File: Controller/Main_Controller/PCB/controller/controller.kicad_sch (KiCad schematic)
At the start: 253 parts, among them J1 Conn_01x10, M1 Motor_DC, Q1 S9013, Q10 S9013, Q11 S9013, Q12 S9013, Q13 S9013, Q14 S9013, Q15 S9013, Q16 S9013, Q17 S9013, Q18 S9013, Q19 S9013, Q2 S9013, Q20 S9013, Q21 S9013, Q22 S9013, Q23 S9013, Q24 S9013, Q25 Q_PMOS_DGS, Q26 Q_NMOS_DGS, Q27 S9013, Q3 S9013, Q4 S9013, Q5 S9013, Q6 S9013, Q7 S9013, Q8 S9013, Q9 S9013, SW1 SW_SPDT, SW2 SW_SPDT, U1 NUCLEO-L432KC, U10 ZLDO1117G50TA, U2 NUCLEO144-F429ZI, U3 74HC14, U4 74HC14, U5 74HC14, U6 Joystick, U7 Joystick, U8 HY1602E, U9 ZSR330GTA

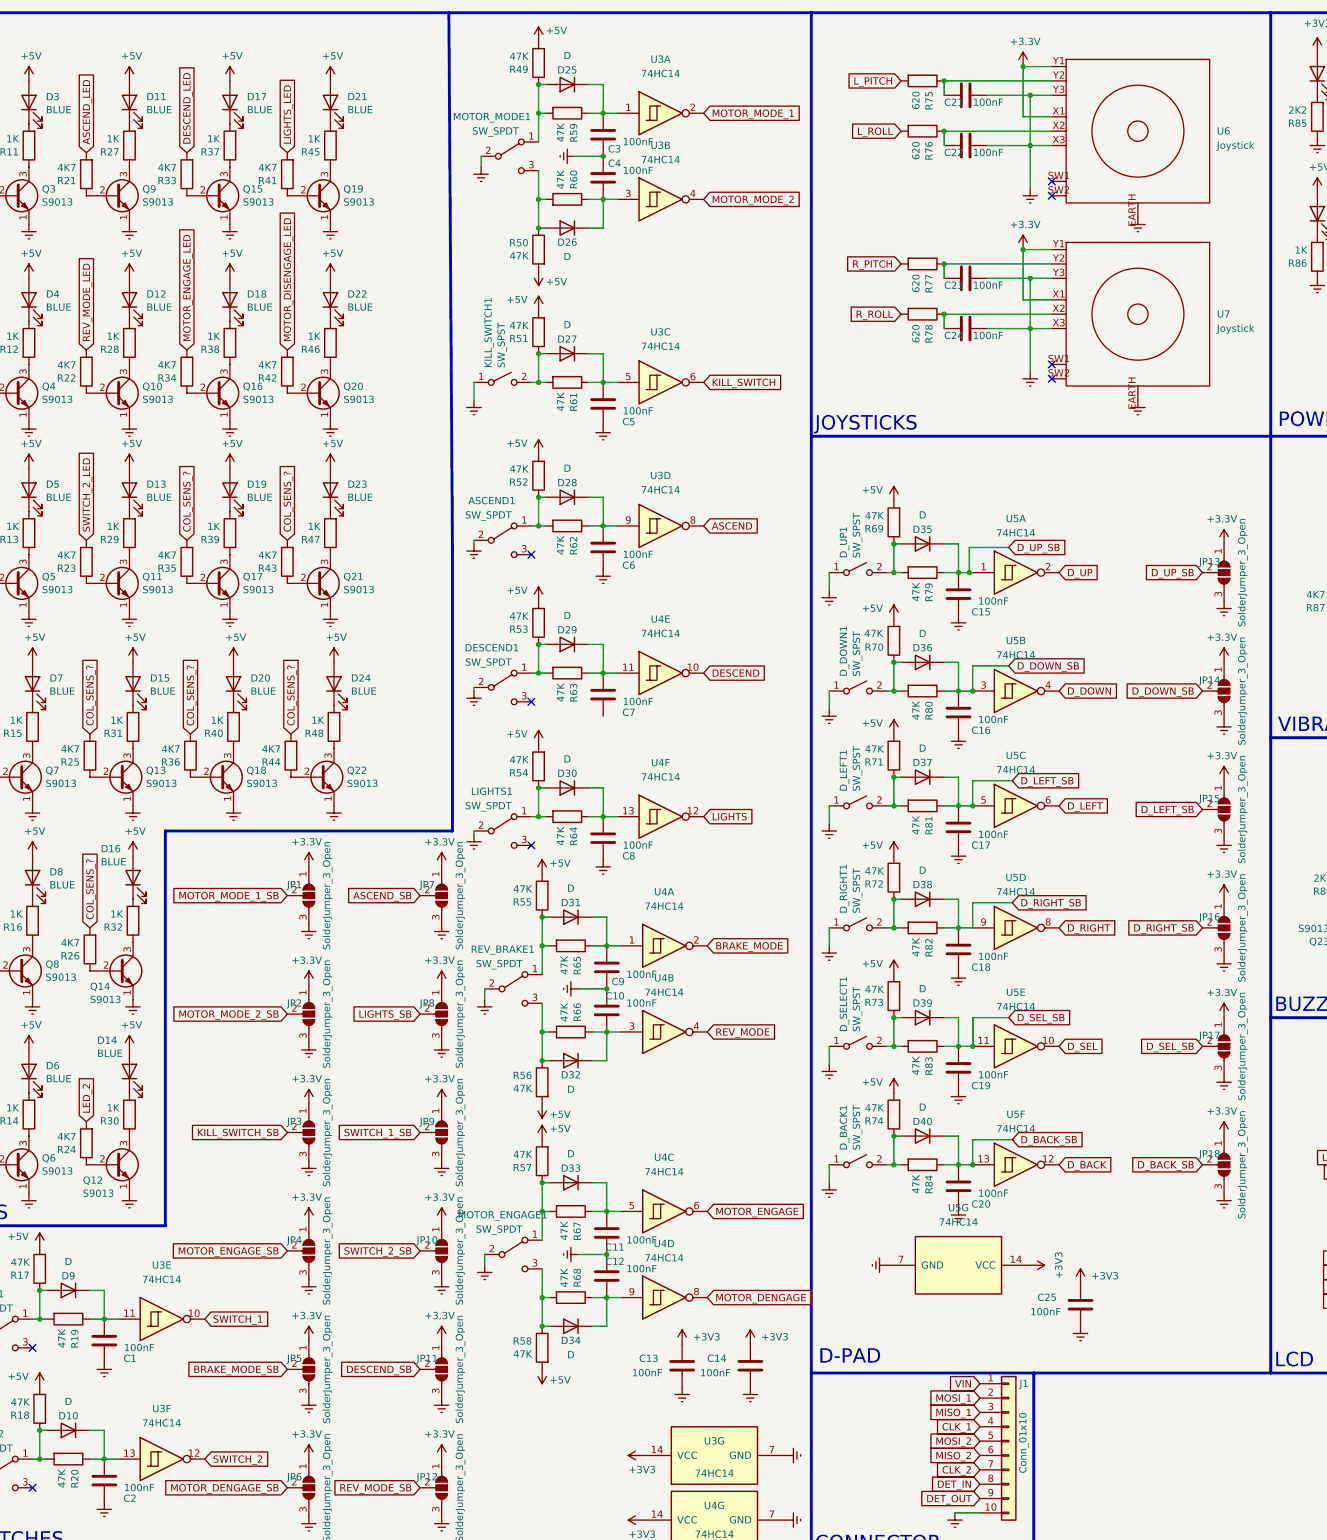
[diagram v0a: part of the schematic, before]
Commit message: Schmitt fixes and label adjustments
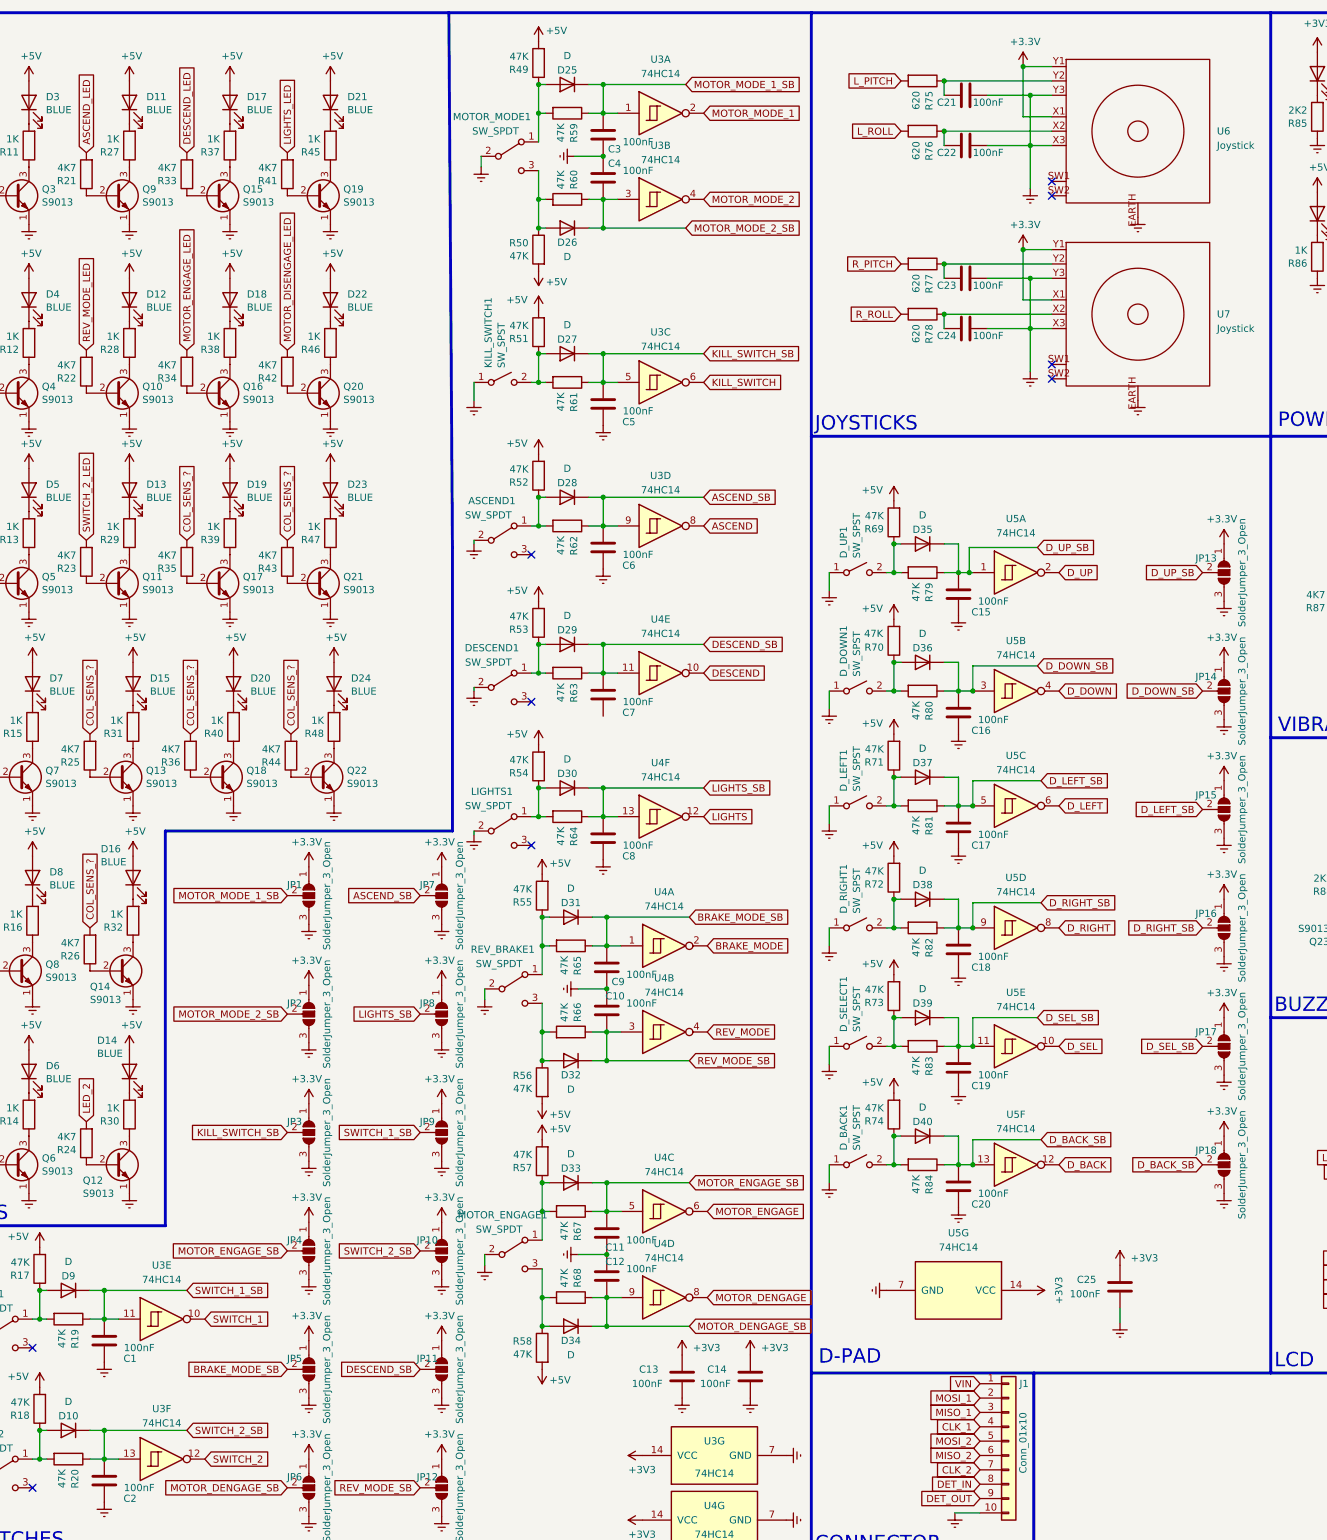
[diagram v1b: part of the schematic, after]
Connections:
- net ASCEND_SB: now also C6.2, D28.1 (K), R62.1, U3.9
- net BRAKE_MODE_SB: now also C9.2, D31.1 (K), R65.1, U4.1
- net DESCEND_SB: now also C7.2, D29.1 (K), R63.1, U4.11
- net KILL_SWITCH_SB: now also C5.2, D27.1 (K), R61.1, U3.5
- net LIGHTS_SB: now also C8.2, D30.1 (K), R64.1, U4.13
- net MOTOR_DENGAGE_SB: now also C12.2, D34.1 (K), R68.1, U4.9
- net MOTOR_ENGAGE_SB: now also C11.2, D33.1 (K), R67.1, U4.5
- net MOTOR_MODE_1_SB: now also C3.2, D25.1 (K), R59.1, U3.1
- net MOTOR_MODE_2_SB: now also C4.2, D26.1 (K), R60.1, U3.3
- net REV_MODE_SB: now also C10.2, D32.1 (K), R66.1, U4.3
- net SWITCH_1_SB: now also C1.2, D9.1 (K), R19.1, U3.11
- net SWITCH_2_SB: now also C2.2, D10.1 (K), R20.1, U3.13
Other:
- moved on the sheet: C13, C14, C25, U5G
